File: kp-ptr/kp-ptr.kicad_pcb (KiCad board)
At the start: 4 copper layers, 31.6 x 101.5 mm, 189 parts, among them IC1 E22-900M22S, J1 ESP32_PROG_CON, J10 Conn_01x10_Male, J11 u.fl, J12 Conn_01x06_Male, J13 Conn_01x02_Male, J2 Conn_01x02, J3 Conn_01x02, J4 USB_C_Receptacle_USB2.0, J5 Conn_01x06_Male, J5 Micro_SD_Card_Det, J6 Conn_01x02, J7 Conn_01x02, J8 Conn_01x02, J9 Conn_01x02, Q10 NMOS_SOT23, Q11 NMOS_SOT23, Q12 PMOS_SOT23, Q13 PMOS_SOT23, Q5 NMOS_SOT23, Q6 NMOS_SOT23, Q7 NMOS_SOT23, Q8 PMOS_SOT23, Q9 PMOS_SOT23, U1 ESP32-S3FN8, U10 USBLC6-2SC6, U11 W25Q128JVS, U2 NL27WZU04DBVT1G, U3 MS560702BA03-50, U4 MMC5983MA, U5 H3LIS331, U6 L76-L, U7 LSM6DSO32, U8 SPX3819M5-L-3-3, U9 NJG1156PCD, Y1 7M40000005-40MHz

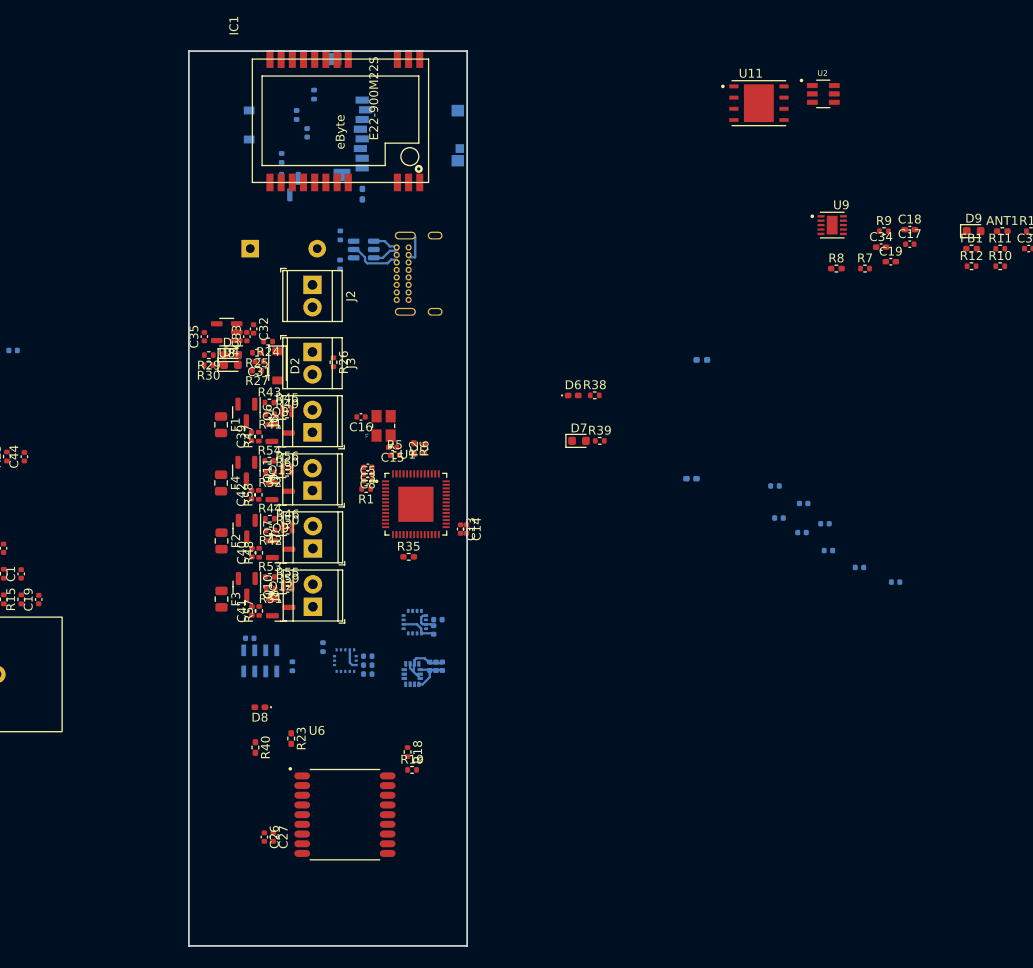
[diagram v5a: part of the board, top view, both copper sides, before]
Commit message: Footprint mosfeta
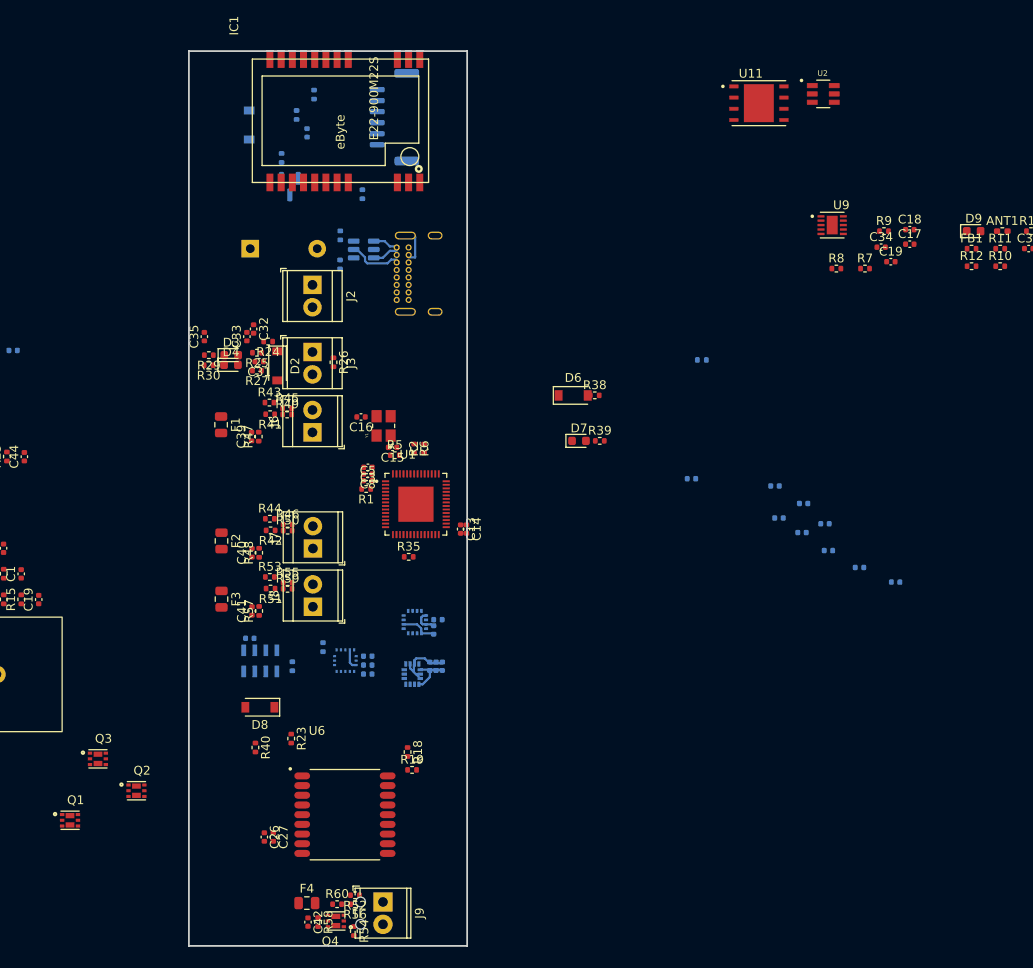
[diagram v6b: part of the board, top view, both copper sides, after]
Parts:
- removed Q10, Q11, Q6, Q7: NMOS_SOT23, Package_TO_SOT_SMD:SOT-23
- removed Q12, Q13, Q8, Q9: PMOS_SOT23, Package_TO_SOT_SMD:SOT-23
- removed U8: SPX3819M5-L-3-3, Package_TO_SOT_SMD:SOT-23-5
- added Q1: DMC2025UFDB_v2, KP-PTR_lib:DMC2025UFDB, F.Cu at (127.3, 122.0)
- added Q2: DMC2025UFDB_v2, KP-PTR_lib:DMC2025UFDB, F.Cu at (134.8, 118.7)
- added Q3: DMC2025UFDB_v2, KP-PTR_lib:DMC2025UFDB, F.Cu at (130.5, 115.1)
- added Q4: DMC2025UFDB_v2, KP-PTR_lib:DMC2025UFDB, F.Cu at (157.5, 133.5)
- C1: value TBD -> 56pF; footprint Capacitor_SMD:C_0402_1005Metric_Pad0.74x0.62mm_HandSolder -> Capacitor_SMD:C_0402_1005Metric
- C18: value 47p -> 1nF; footprint Capacitor_SMD:C_0402_1005Metric_Pad0.74x0.62mm_HandSolder -> Capacitor_SMD:C_0402_1005Metric
- C19: footprint Capacitor_SMD:C_0402_1005Metric_Pad0.74x0.62mm_HandSolder -> Capacitor_SMD:C_0402_1005Metric
- C34: value 100n -> DNP; footprint Capacitor_SMD:C_0402_1005Metric_Pad0.74x0.62mm_HandSolder -> Capacitor_SMD:C_0402_1005Metric
- D6: value LED -> TBD; footprint LED_SMD:LED_0402_1005Metric_Pad0.77x0.64mm_HandSolder -> Diode_SMD:D_SOD-123
- D8: value LED -> D_Schottky; footprint LED_SMD:LED_0402_1005Metric_Pad0.77x0.64mm_HandSolder -> Diode_SMD:D_SOD-123
- FB1: value TBD -> 200mA; footprint Resistor_SMD:R_0402_1005Metric_Pad0.72x0.64mm_HandSolder -> Resistor_SMD:R_0402_1005Metric
- J5: value Micro_SD_Card_Det -> Conn_01x06_Male; footprint KP-PTR_lib:GCT_MEM2051-00-195-00-A -> Connector_JST:JST_GH_BM06B-GHS-TBT_1x06-1MP_P1.25mm_Vertical
- J9: footprint TerminalBlock_TE-Connectivity:TerminalBlock_TE_282834-2_1x02_P2.54mm_Horizontal -> TerminalBlock_Phoenix:TerminalBlock_Phoenix_MPT-0,5-2-2.54_1x02_P2.54mm_Horizontal
- R23: value DNP -> 10k; footprint Resistor_SMD:R_0402_1005Metric_Pad0.72x0.64mm_HandSolder -> Resistor_SMD:R_0402_1005Metric
- R34, R35, R36: value 100k -> 1k; footprint Resistor_SMD:R_0402_1005Metric_Pad0.72x0.64mm_HandSolder -> Resistor_SMD:R_0402_1005Metric
- R40: footprint Resistor_SMD:R_0402_1005Metric_Pad0.72x0.64mm_HandSolder -> Resistor_SMD:R_0402_1005Metric
- R6: value 10k -> 1k; footprint Resistor_SMD:R_0402_1005Metric_Pad0.72x0.64mm_HandSolder -> Resistor_SMD:R_0402_1005Metric
- R8: value 10R -> 1k; footprint Resistor_SMD:R_0402_1005Metric_Pad0.72x0.64mm_HandSolder -> Resistor_SMD:R_0402_1005Metric
- moved R54 54.2 mm to (159.5, 134.6), turned to -90 degrees
- moved R56 50.3 mm to (159.6, 131.6), turned to 180 degrees
- moved R60 49.3 mm to (157.6, 131.6)
- moved R58 49.0 mm to (155.4, 133.6), turned to -90 degrees
- moved R52 48.9 mm to (159.6, 130.6)
- moved C42 48.9 mm to (154.3, 133.6), turned to -90 degrees
- moved F4 48.7 mm to (154.2, 131.4), turned to 0 degrees
- moved J9 47.4 mm to (162.8, 131.3), turned to -90 degrees
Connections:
- C1 pad 1: Net-(U9-Pad10) -> Net-(C1-Pad1)
- C1 pad 2: Net-(U6-Pad11) -> Net-(C1-Pad2)
- C1 pad 2: Earth -> Net-(C1-Pad2)
- C18 pad 1: Net-(C18-Pad1) -> Earth
- C18 pad 2: unconnected-(C18-Pad2) -> +3.3VADC
- C19 pad 1: Net-(C18-Pad1) -> Net-(C1-Pad1)
- C19 pad 1: Net-(U9-Pad10) -> Net-(C1-Pad1)
- C34 pad 1: Net-(U9-Pad5) -> Net-(C34-Pad1)
- C34 pad 2: Earth -> Net-(C19-Pad2)
- C43 pad 2: Net-(U9-Pad5) -> Net-(C34-Pad1)
- D6 pad 2: Net-(D6-Pad2) -> Net-(ANT3-Pad1)
- D8 pad 1: Earth -> VDD
- D8 pad 2: Net-(D8-Pad2) -> VBUS
- FB1 pad 1: Net-(C37-Pad1) -> +3V3
- FB1 pad 2: +3V3 -> +3.3VADC
- J10 pad 4: Net-(R35-Pad1) -> Net-(J10-Pad4)
- J10 pad 5: Net-(R36-Pad1) -> Net-(J10-Pad5)
- J10 pad 6: Net-(R40-Pad1) -> Net-(J10-Pad6)
- J5 pad 1: Net-(J5-Pad1) -> +5V
- J5 pad 2: SPI_CS_SDCARD -> UART1_OUT
- J5 pad 3: SPI_MOSI -> UART1_IN
- J5 pad 4: Net-(C37-Pad1) -> I2C_SCL
- J5 pad 5: SPI_CLK -> I2C_SDA
- R23 pad 1: +3V3 -> Net-(D11-Pad1)
- R23 pad 2: Net-(R23-Pad2) -> Earth
- R34 pad 1: SPI_MOSI -> Net-(D12-Pad2)
- R34 pad 2: +3V3 -> SERVO_EN
- R35 pad 1: Net-(R35-Pad1) -> Net-(J10-Pad4)
- R35 pad 1: SPI_MISO -> Net-(J10-Pad4)
- R35 pad 2: +3V3 -> SERVO_1
- R36 pad 1: Net-(R36-Pad1) -> Net-(J10-Pad5)
- R36 pad 1: Net-(J5-Pad8) -> Net-(J10-Pad5)
- R36 pad 2: +3V3 -> SERVO_2
- R40 pad 1: Net-(R40-Pad1) -> Net-(J10-Pad6)
- R40 pad 1: Net-(D8-Pad2) -> Net-(J10-Pad6)
- R40 pad 2: LED3 -> SERVO_3
- R6 pad 1: Earth -> CHIP_PU
- R6 pad 2: Net-(R6-Pad2) -> Net-(J1-Pad5)
- R8 pad 1: +3V3 -> U0RXD
- R8 pad 2: Net-(C34-Pad1) -> Net-(J1-Pad2)
- U6 pad 11: Net-(U6-Pad11) -> Net-(C1-Pad2)
- U9 pad 10: Net-(U9-Pad10) -> Net-(C1-Pad1)
- U9 pad 5: Net-(U9-Pad5) -> Net-(C34-Pad1)
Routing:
- net VBUS: track 9.67 -> 3.88 mm
- net Earth: track 12.9 -> 18.7 mm

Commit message: Grupowanie
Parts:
- removed the C1 at (197.8, 83.3)
- removed the C18 at (222.6, 55.0)
- removed the C19 at (220.4, 58.7)
- removed the C34 at (117.8, 90.0)
- removed the D6 at (114.5, 95.6)
- removed the D8 at (114.5, 79.3)
- removed F6: 500mA, Fuse:Fuse_0805_2012Metric
- removed the FB1 at (229.6, 57.2)
- removed the J5 at (94.2, 88.0)
- removed L5: 10nH, Inductor_SMD:L_0402_1005Metric
- removed the R23 at (120.1, 80.8)
- removed the R34 at (199.0, 69.8)
- removed the R35 at (106.6, 107.0)
- removed the R36 at (160.5, 51.0)
- removed the R40 at (148.3, 113.8)
- removed the R6 at (98.4, 73.4)
- removed the R8 at (214.3, 59.4)
- added F1: 500mA, Fuse:Fuse_0805_2012Metric, F.Cu at (118.2, 68.6)
- added L3: 10nH, Inductor_SMD:L_0402_1005Metric, F.Cu at (155.3, 66.8)
- ANT2: renamed from ANT3; moved to B.Cu
- C1: renamed from C2; moved to F.Cu
- C10: renamed from C11; moved to F.Cu
- C11: renamed from C12; moved to F.Cu
- C16: renamed from C20; moved to F.Cu
- C17: renamed from C21; moved to F.Cu
- C18: renamed from C22; moved to F.Cu
- C20: renamed from C23; moved to F.Cu
- C21: renamed from C24; moved to F.Cu
- C22: renamed from C25; moved to F.Cu
- C28, C29, J4, LS1, U7: moved to F.Cu
- C3: renamed from C4; moved to F.Cu
- C31: renamed from C30; moved to F.Cu
- C39: renamed from C37; moved to F.Cu
- C43: renamed from C38; moved to F.Cu
- C5: renamed from C6; moved to F.Cu
- C6: renamed from C7; moved to F.Cu
- C8: renamed from C9; moved to F.Cu
- C9: renamed from C10; moved to F.Cu
- D11: renamed from D5; moved to F.Cu
- J10: renamed from J6; footprint TerminalBlock_TE-Connectivity:TerminalBlock_TE_282834-2_1x02_P2.54mm_Horizontal -> TerminalBlock_Phoenix:TerminalBlock_Phoenix_MPT-0,5-2-2.54_1x02_P2.54mm_Horizontal
- J11: renamed from J7; footprint TerminalBlock_TE-Connectivity:TerminalBlock_TE_282834-2_1x02_P2.54mm_Horizontal -> TerminalBlock_Phoenix:TerminalBlock_Phoenix_MPT-0,5-2-2.54_1x02_P2.54mm_Horizontal; moved to B.Cu
- J12: renamed from J8; footprint TerminalBlock_TE-Connectivity:TerminalBlock_TE_282834-2_1x02_P2.54mm_Horizontal -> TerminalBlock_Phoenix:TerminalBlock_Phoenix_MPT-0,5-2-2.54_1x02_P2.54mm_Horizontal
- J13: renamed from J9; moved to B.Cu
- J2, J3: footprint TerminalBlock_TE-Connectivity:TerminalBlock_TE_282834-2_1x02_P2.54mm_Horizontal -> TerminalBlock_Phoenix:TerminalBlock_Phoenix_MPT-0,5-2-2.54_1x02_P2.54mm_Horizontal
- J6: renamed from J5; moved to F.Cu
- Q1: renamed from Q5; moved to F.Cu
- R10: renamed from R17; moved to F.Cu
- R15: renamed from R20; moved to F.Cu
- R26: renamed from R32; moved to F.Cu
- R27: renamed from R33; moved to F.Cu
- R42: renamed from R37; moved to F.Cu
- R6: renamed from R3; moved to F.Cu
- R7: renamed from R4; moved to F.Cu
- U2: renamed from U3; moved to F.Cu
- U3: renamed from U4; moved to F.Cu
- U4: renamed from U5; moved to F.Cu
- U9: renamed from U10; moved to F.Cu
- moved C19 243.4 mm to (-11.8, -9.00), turned to 90 degrees
- moved R9 234.4 mm to (-6.20, -10.6), turned to 90 degrees
- moved R18 233.0 mm to (-6.80, 0.60), turned to 90 degrees
- moved C16 211.3 mm to (-11.0, -11.4), turned to 90 degrees
- moved C28 210.6 mm to (-12.4, -1.39)
- moved C17 210.3 mm to (-10.8, -9.36)
- moved C29 209.3 mm to (-11.7, -1.39)
- moved C31 208.1 mm to (-11.0, -1.39)
- moved C41 207.5 mm to (30.1, 32.2), turned to -90 degrees
- moved U3 206.7 mm to (-8.65, -10.2), turned to 180 degrees
- moved C8 205.7 mm to (42.9, -7.98), turned to 0 degrees
- moved R28 205.2 mm to (29.7, 30.6), turned to 180 degrees
- moved U7 204.7 mm to (-9.00, -0.50)
- moved D8 200.7 mm to (30.9, 29.0), turned to 180 degrees
- moved R31 195.1 mm to (37.8, 51.6), turned to 90 degrees
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- renumbered ANT2 to ANT1, ANT1 to ANT3, C13 to C12, C14 to C13, C15 to C14, C16 to C15, C17 to C19, C3 to C2, C26 to C23, C27 to C24, C1 to C25, C18 to C26, C19 to C27, C34 to C30, C43 to C32, C31 to C33, C32 to C34, C33 to C35, C44 to C36, C35 to C37, C45 to C38, C5 to C4, C46 to C40, C36 to C41, C47 to C42, C48 to C44, C49 to C45, C50 to C46, C39 to C47, C40 to C48, C41 to C49, C42 to C50, C8 to C7, D12 to D10, D7 to D12, D6 to D2, D8 to D3, D2 to D4, D3 to D5, D4 to D6, D11 to D7, D9 to D8, D10 to D9, F1 to F2, F2 to F3, F3 to F4, F4 to F5, J11 to J5, J10 to J7, J12 to J8, J13 to J9, L2 to L1, L3 to L2, Q1 to Q2, Q2 to Q3, Q3 to Q4, Q4 to Q5, R2 to R1, R18 to R11, R15 to R12, R19 to R13, R16 to R14, R21 to R16, R22 to R17, R9 to R18, R24 to R19, R6 to R2, R25 to R20, R26 to R21, R27 to R22, R29 to R23, R30 to R24, R23 to R25, R10 to R28, R28 to R29, R8 to R3, R31 to R30, R11 to R31, R12 to R32, R13 to R33, R40 to R37, R61 to R38, R62 to R39, R14 to R4, R38 to R40, R39 to R41, R63 to R43, R41 to R44, R42 to R45, R43 to R46, R44 to R47, R45 to R48, R46 to R49, R1 to R5, R47 to R50, R48 to R51, R49 to R52, R50 to R53, R51 to R54, R52 to R55, R53 to R56, R54 to R57, R55 to R58, R56 to R59, R57 to R60, R58 to R61, R59 to R62, R60 to R63, R5 to R8, R7 to R9, U11 to U10, U2 to U11, U6 to U5, U9 to U6
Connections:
- D11 pad 2: Net-(D5-Pad2) -> Net-(D11-Pad2)
- LS1 pad 1: (no net) -> +3V3
- LS1 pad 2: (no net) -> Net-(D11-Pad2)
- Q1 pad 3: Net-(D5-Pad2) -> Net-(D11-Pad2)
- U6 pad 6: (no net) -> Earth
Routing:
- net unconnected-(J4-PadA5): track 5.95 -> 0.00 mm
- net Net-(J4-PadA7): track 0.00 -> 5.79 mm
- net VBUS: track 3.88 -> 5.95 mm
- net Earth: track 18.7 -> 16.8 mm
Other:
- outline, holes or cut-outs redrawn

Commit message: 1 proba zmieszczenia wszystkiego
Signed-off-by: kretu <krecik@gmail.com>
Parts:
- J2: footprint TerminalBlock_Phoenix:TerminalBlock_Phoenix_MPT-0,5-2-2.54_1x02_P2.54mm_Horizontal -> Connector_JST:JST_GH_SM02B-GHS-TB_1x02-1MP_P1.25mm_Horizontal
- J9: footprint TerminalBlock_TE-Connectivity:TerminalBlock_TE_282834-2_1x02_P2.54mm_Horizontal -> Connector_JST:JST_GH_BM02B-GHS-TBT_1x02-1MP_P1.25mm_Vertical
- moved C16 188.5 mm to (174.2, 24.0)
- moved C17 188.5 mm to (174.4, 26.0)
- moved C19 188.5 mm to (173.4, 26.4)
- moved U3 188.5 mm to (176.5, 25.1)
- moved R9 188.5 mm to (179.0, 24.8)
- moved C39 145.2 mm to (179.0, 82.0)
- moved R26 145.2 mm to (181.0, 77.2)
- moved C40 145.2 mm to (178.0, 82.0)
- moved R27 145.2 mm to (187.4, 80.7)
- moved U10 145.2 mm to (183.2, 80.6)
- moved ANT3 120.2 mm to (165.0, 44.1)
- moved C43 120.2 mm to (147.6, 42.7)
- moved D8 120.2 mm to (150.7, 19.3)
- moved FB2 120.2 mm to (146.6, 45.3)
- moved R29 120.2 mm to (152.6, 41.9)
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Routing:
- net Earth: track 16.8 -> 12.9 mm
- net VBUS: track 5.95 -> 9.83 mm
- net Net-(J4-PadA7): track 5.79 -> 2.94 mm
- net Net-(J4-PadA6): track 0.00 -> 2.85 mm
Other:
- board size 31.6 x 101.5 mm -> 31.6 x 104.6 mm
